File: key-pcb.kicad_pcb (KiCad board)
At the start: 2 copper layers, 3.6 x 3.3 mm, 24 parts, among them J1 row left, J10 DIN bottom, J11 DOUT bottom, J12 VDD bottom, J13 VSS left, J14 DOUT left, J15 DIN left, J16 VDD left, J17 VDD right, J18 DOUT right, J19 DIN right, J2 row right, J20 VSS right, J3 col top, J4 col bottom, J5 VDD top, J6 DIN top, J7 DOUT top, J8 VSS top, J9 VSS bottom

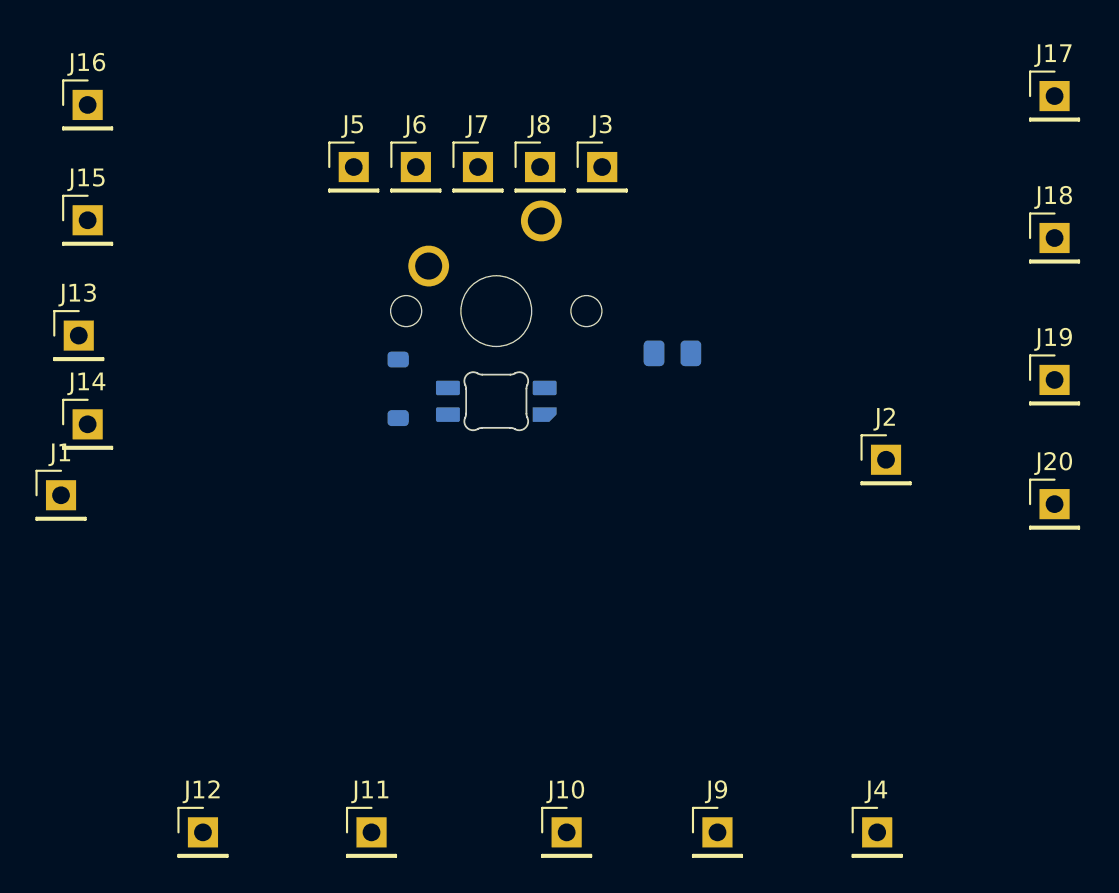
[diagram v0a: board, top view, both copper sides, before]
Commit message: Routed, but DRC violation
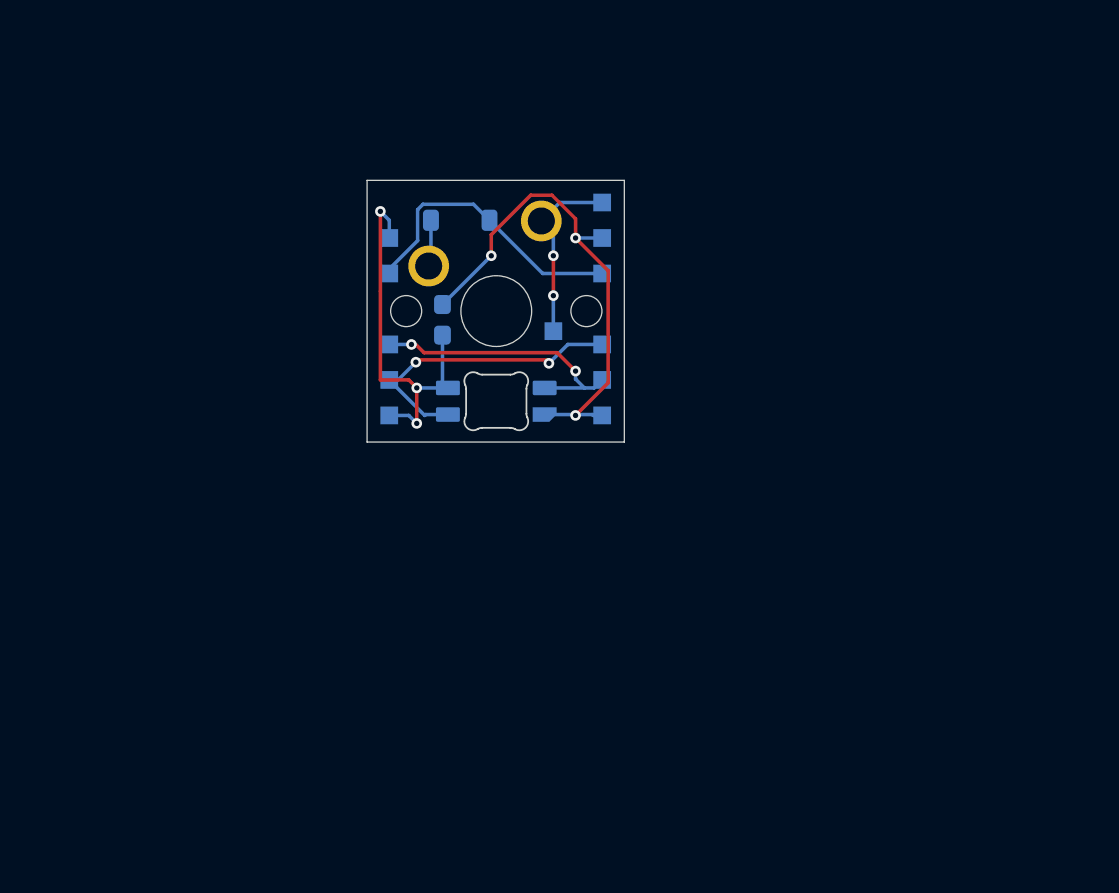
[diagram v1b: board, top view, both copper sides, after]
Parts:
- removed J10: DIN bottom, Connector_PinHeader_2.54mm:PinHeader_1x01_P2.54mm_Vertical
- removed J11: DOUT bottom, Connector_PinHeader_2.54mm:PinHeader_1x01_P2.54mm_Vertical
- removed J13: VSS left, Connector_PinHeader_2.54mm:PinHeader_1x01_P2.54mm_Vertical
- removed J16: VDD left, Connector_PinHeader_2.54mm:PinHeader_1x01_P2.54mm_Vertical
- removed J17: VDD right, Connector_PinHeader_2.54mm:PinHeader_1x01_P2.54mm_Vertical
- removed J20: VSS right, Connector_PinHeader_2.54mm:PinHeader_1x01_P2.54mm_Vertical
- removed J6: DIN top, Connector_PinHeader_2.54mm:PinHeader_1x01_P2.54mm_Vertical
- removed J7: DOUT top, Connector_PinHeader_2.54mm:PinHeader_1x01_P2.54mm_Vertical
- C1: footprint Capacitor_SMD:C_0805_2012Metric_Pad1.18x1.45mm_HandSolder -> Capacitor_SMD:C_0603_1608Metric_Pad1.08x0.95mm_HandSolder
- J1, J12, J14, J15, J18, J19, J2, J3, J4, J5, J8, J9: footprint Connector_PinHeader_2.54mm:PinHeader_1x01_P2.54mm_Vertical -> TestPoint:TestPoint_Pad_1.0x1.0mm; moved to B.Cu
- moved J4 33.6 mm to (141.2, 97.8), turned to 180 degrees
- moved J18 26.2 mm to (144.0, 98.5), turned to 180 degrees
- moved J12 25.7 mm to (132.0, 102.5), turned to 180 degrees
- moved J19 25.5 mm to (144.0, 100.5), turned to 180 degrees
- moved J9 24.4 mm to (144.0, 102.5), turned to 180 degrees
- moved J1 22.3 mm to (132.0, 94.5), turned to 180 degrees
- moved J2 19.1 mm to (144.0, 94.5), turned to 180 degrees
- moved J15 18.4 mm to (132.0, 98.5), turned to 180 degrees
- moved J14 17.2 mm to (132.0, 100.5), turned to 180 degrees
- moved C1 13.1 mm to (135.0, 97.1), turned to -90 degrees
- moved D1 10.1 mm to (136.0, 91.5), turned to 180 degrees
- moved J8 5.32 mm to (144.0, 92.5), turned to 180 degrees
- moved J5 4.47 mm to (132.0, 92.5), turned to 180 degrees
- moved J3 2.00 mm to (144.0, 90.5), turned to 180 degrees
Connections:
- net GND renamed VSS
- net Net-(D1-K) renamed /row
- net Net-(J10-Pin_1) renamed /DIN
- net Net-(J11-Pin_1) renamed /DOUT
- net Net-(J12-Pin_1) renamed VDD
- net Net-(J3-Pin_1) renamed /col
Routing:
- net VSS: track 0.00 -> 29.3 mm, vias 0 -> 3
- net VDD: track 0.00 -> 22.2 mm, vias 0 -> 3
- net /DOUT: track 0.00 -> 17.3 mm, vias 0 -> 2
- net /row: track 0.00 -> 16.4 mm
- net /DIN: track 0.00 -> 15.5 mm, vias 0 -> 2
- net /col: track 0.00 -> 10.3 mm, vias 0 -> 2
- net Net-(D1-A): track 0.00 -> 2.63 mm
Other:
- board size 3.6 x 3.3 mm -> 14.5 x 14.8 mm

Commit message: Passing all DRC
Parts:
- renumbered J5 to +, J12 to +, J8 to -, J9 to -, D1 to D, J19 to IN, J15 to IN, LED1 to LED, J18 to OUT, J14 to OUT, J4 to c, J3 to c, C1 to cap, J1 to r, J2 to r
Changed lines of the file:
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@@
 		(descr "Add-on for regular MX-footprints with 6028 reverse mount LED")
 		(tags "cherry MX 6028 rearmount rear mount led rgb backlight")
-		(property "Reference" "LED1"
-			(at 0.5 -2.6 0)
-			(layer "B.SilkS")
-			(effects
-				(font
-					(size 1 1)
-					(thickness 0.15)
+		(property "Reference" "LED"
+			(at 0.0325 2.2 0)
+			(layer "B.SilkS")
+			(effects
+				(font
+					(size 0.8 0.8)
+					(thickness 0.125)
 				)
 				(justify mirror)
@@
 		(descr "SMD rectangular pad as test Point, square 1.0mm side length")
 		(tags "test point SMD pad rectangle square")
-		(property "Reference" "J19"
-			(at 0 1.448 0)
-			(layer "B.SilkS")
-			(effects
-				(font
-					(size 1 1)
-					(thickness 0.15)
+		(property "Reference" "IN"
+			(at 1.5 0 0)
+			(layer "B.SilkS")
+			(effects
+				(font
+					(size 0.8 0.8)
+					(thickness 0.125)
+					(bold yes)
 				)
 				(justify mirror)
@@
 		(descr "SMD rectangular pad as test Point, square 1.0mm side length")
 		(tags "test point SMD pad rectangle square")
-		(property "Reference" "J18"
-			(at 0 1.448 0)
-			(layer "B.SilkS")
-			(effects
-				(font
-					(size 1 1)
-					(thickness 0.15)
+		(property "Reference" "OUT"
+			(at 2 -0.75 0)
+			(layer "B.SilkS")
+			(effects
+				(font
+					(size 0.8 0.8)
+					(thickness 0.125)
+					(bold yes)
 				)
 				(justify mirror)
@@
 		(descr "Capacitor SMD 0603 (1608 Metric), square (rectangular) end terminal, IPC-7351 nominal with elongated pad for handsoldering. (Body size source: IPC-SM-782 page 76, https://www.pcb-3d.com/wordpress/wp-content/uploads/ipc-sm-782a_amendment_1_and_2.pdf), generated with kicad-footprint-generator")
 		(tags "capacitor handsolder")
-		(property "Reference" "C1"
-			(at 0 1.43 90)
-			(layer "B.SilkS")
-			(effects
-				(font
-					(size 1 1)
-					(thickness 0.15)
+		(property "Reference" "cap"
+			(at -2.6125 -0.75 90)
+			(layer "B.SilkS")
+			(effects
+				(font
+					(size 0.8 0.8)
+					(thickness 0.125)
+					(bold yes)
 				)
 				(justify mirror)
@@
 		(descr "SMD rectangular pad as test Point, square 1.0mm side length")
 		(tags "test point SMD pad rectangle square")
-		(property "Reference" "J8"
-			(at 0 1.448 0)
-			(layer "B.SilkS")
-			(effects
-				(font
-					(size 1 1)
-					(thickness 0.15)
+		(property "Reference" "-"
+			(at 1.5 0 0)
+			(layer "B.SilkS")
+			(effects
+				(font
+					(size 0.8 0.8)
+					(thickness 0.125)
 				)
 				(justify mirror)
@@
 		(descr "SMD rectangular pad as test Point, square 1.0mm side length")
 		(tags "test point SMD pad rectangle square")
-		(property "Reference" "J1"
-			(at 0 1.448 0)
-			(layer "B.SilkS")
-			(effects
-				(font
-					(size 1 1)
-					(thickness 0.15)
+		(property "Reference" "r"
+			(at -1 -0.539554 0)
+			(layer "B.SilkS")
+			(effects
+				(font
+					(size 0.8 0.8)
+					(thickness 0.125)
+					(bold yes)
 				)
 				(justify mirror)
@@
 		(descr "SMD rectangular pad as test Point, square 1.0mm side length")
 		(tags "test point SMD pad rectangle square")
-		(property "Reference" "J5"
-			(at 0 1.448 0)
-			(layer "B.SilkS")
-			(effects
-				(font
-					(size 1 1)
-					(thickness 0.15)
+		(property "Reference" "+"
+			(at -1.25 0 0)
+			(layer "B.SilkS")
+			(effects
+				(font
+					(size 0.8 0.8)
+					(thickness 0.125)
+					(bold yes)
 				)
 				(justify mirror)
@@
 		(descr "SMD rectangular pad as test Point, square 1.0mm side length")
 		(tags "test point SMD pad rectangle square")
-		(property "Reference" "J9"
-			(at 0 1.448 0)
-			(layer "B.SilkS")
-			(effects
-				(font
-					(size 1 1)
-					(thickness 0.15)
+		(property "Reference" "-"
+			(at 1.75 0 0)
+			(layer "B.SilkS")
+			(effects
+				(font
+					(size 0.8 0.8)
+					(thickness 0.125)
+					(bold yes)
 				)
 				(justify mirror)
@@
 		(descr "SMD rectangular pad as test Point, square 1.0mm side length")
 		(tags "test point SMD pad rectangle square")
-		(property "Reference" "J4"
+		(property "Reference" "c"
 			(at 0 1.448 0)
 			(layer "B.SilkS")
 			(effects
 				(font
-					(size 1 1)
-					(thickness 0.15)
+					(size 0.8 0.8)
+					(thickness 0.125)
+					(bold yes)
 				)
 				(justify mirror)
@@
 		(descr "SMD rectangular pad as test Point, square 1.0mm side length")
 		(tags "test point SMD pad rectangle square")
-		(property "Reference" "J12"
-			(at 0 1.448 0)
-			(layer "B.SilkS")
-			(effects
-				(font
-					(size 1 1)
-					(thickness 0.15)
+		(property "Reference" "+"
+			(at -1.5 0.5 0)
+			(layer "B.SilkS")
+			(effects
+				(font
+					(size 0.8 0.8)
+					(thickness 0.125)
+					(bold yes)
 				)
 				(justify mirror)
@@
 		(descr "SMD rectangular pad as test Point, square 1.0mm side length")
 		(tags "test point SMD pad rectangle square")
-		(property "Reference" "J15"
-			(at 0 1.448 0)
-			(layer "B.SilkS")
-			(effects
-				(font
-					(size 1 1)
-					(thickness 0.15)
+		(property "Reference" "IN"
+			(at -1.75 0.5 0)
+			(layer "B.SilkS")
+			(effects
+				(font
+					(size 0.8 0.8)
+					(thickness 0.125)
+					(bold yes)
 				)
 				(justify mirror)
@@
 		(descr "SMD rectangular pad as test Point, square 1.0mm side length")
 		(tags "test point SMD pad rectangle square")
-		(property "Reference" "J2"
-			(at 0 1.448 0)
-			(layer "B.SilkS")
-			(effects
-				(font
-					(size 1 1)
-					(thickness 0.15)
+		(property "Reference" "r"
+			(at 1.5 0 0)
+			(layer "B.SilkS")
+			(effects
+				(font
+					(size 0.8 0.8)
+					(thickness 0.125)
+					(bold yes)
 				)
 				(justify mirror)
@@
 		(descr "SMD rectangular pad as test Point, square 1.0mm side length")
 		(tags "test point SMD pad rectangle square")
-		(property "Reference" "J14"
-			(at 0 1.448 0)
-			(layer "B.SilkS")
-			(effects
-				(font
-					(size 1 1)
-					(thickness 0.15)
+		(property "Reference" "OUT"
+			(at -2 0.5 0)
+			(layer "B.SilkS")
+			(effects
+				(font
+					(size 0.8 0.8)
+					(thickness 0.125)
+					(bold yes)
 				)
 				(justify mirror)
@@
 		(descr "SMD rectangular pad as test Point, square 1.0mm side length")
 		(tags "test point SMD pad rectangle square")
-		(property "Reference" "J3"
-			(at 0 1.448 0)
-			(layer "B.SilkS")
-			(effects
-				(font
-					(size 1 1)
-					(thickness 0.15)
+		(property "Reference" "c"
+			(at 1.25 0 0)
+			(layer "B.SilkS")
+			(effects
+				(font
+					(size 0.8 0.8)
+					(thickness 0.125)
 				)
 				(justify mirror)
@@
 		(descr "SOD-123")
 		(tags "SOD-123")
-		(property "Reference" "D1"
-			(at 0 2 0)
-			(layer "B.SilkS")
-			(effects
-				(font
-					(size 1 1)
-					(thickness 0.15)
-				)
-				(justify mirror)
+		(property "Reference" "D"
+			(at 0 0 0)
+			(layer "B.SilkS")
+			(effects
+				(font
+					(size 0.8 0.8)
+					(thickness 0.125)
+					(bold yes)
+				)
+				(justify mirror)

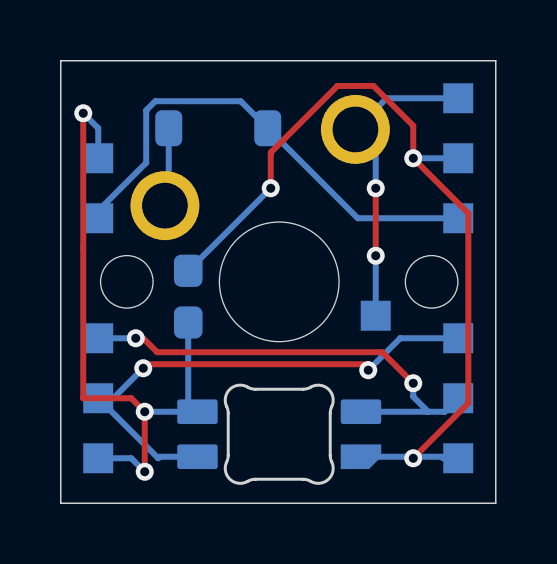
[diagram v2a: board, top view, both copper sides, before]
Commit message: Smaller board
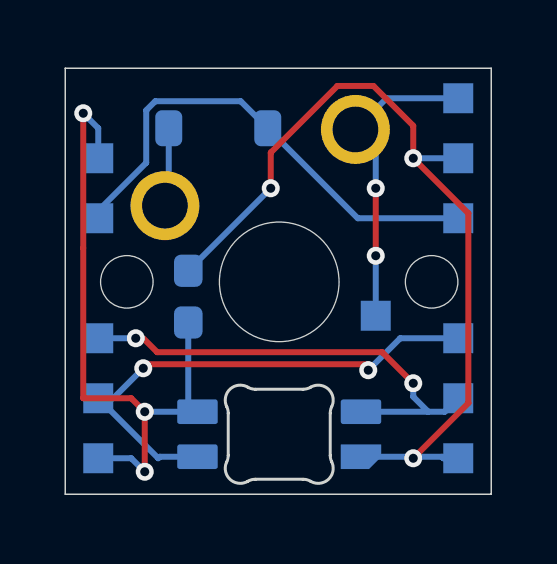
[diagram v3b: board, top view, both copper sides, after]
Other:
- board size 14.5 x 14.8 mm -> 14.2 x 14.2 mm
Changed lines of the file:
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@@
 	)
 	(gr_line
-		(start 130.75 89.25)
-		(end 145.25 89.25)
+		(start 130.9 89.5)
+		(end 145.1 89.5)
 		(stroke
 			(width 0.05)
@@
 	)
 	(gr_line
-		(start 145.25 104)
-		(end 130.75 104)
+		(start 145.1 103.699999)
+		(end 130.9 103.699999)
 		(stroke
 			(width 0.05)
@@
 	)
 	(gr_line
-		(start 145.25 89.25)
-		(end 145.25 104)
+		(start 145.1 89.5)
+		(end 145.1 103.699999)
 		(stroke
 			(width 0.05)
@@
 	)
 	(gr_line
-		(start 130.75 104)
-		(end 130.75 89.25)
+		(start 130.9 103.7)
+		(end 130.9 89.5)
 		(stroke
 			(width 0.05)

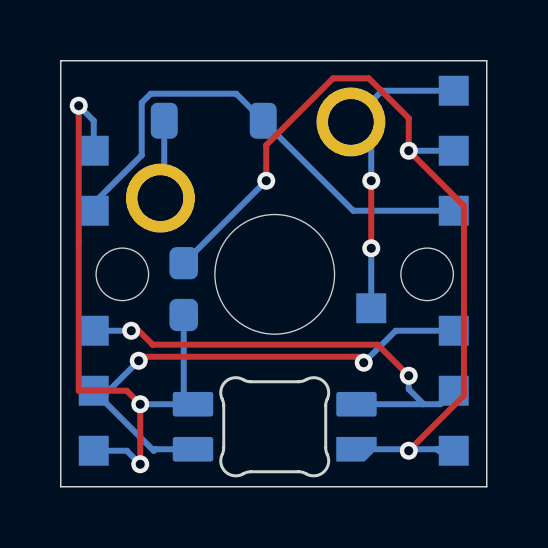
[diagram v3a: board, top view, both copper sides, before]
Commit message: Ground fill
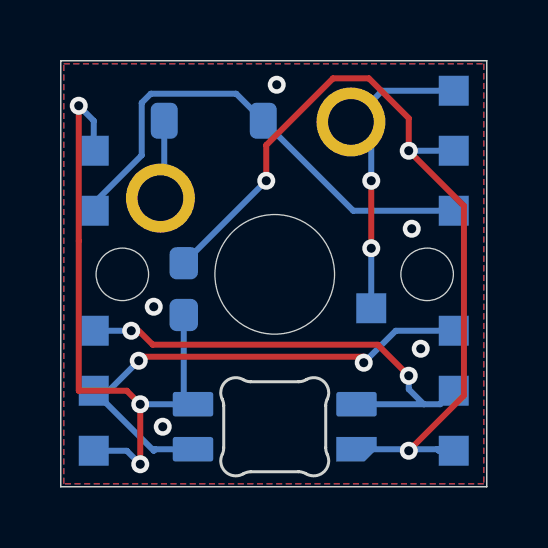
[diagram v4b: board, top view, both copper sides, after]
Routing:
- net VSS: vias 3 -> 8
- added copper zone on B.Cu, net VSS
- added copper zone on F.Cu, net VSS
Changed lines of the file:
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@@
+	)
+	(via
+		(at 142.9 99.1)
+		(size 0.6)
+		(drill 0.3)
+		(layers "F.Cu" "B.Cu")
+		(free yes)
+		(net 6)
 	)
 	(via
@@
 		(drill 0.3)
 		(layers "F.Cu" "B.Cu")
+		(net 6)
+	)
+	(via
+		(at 134.3 101.7)
+		(size 0.6)
+		(drill 0.3)
+		(layers "F.Cu" "B.Cu")
+		(free yes)
+		(net 6)
+	)
+	(via
+		(at 142.6 95.1)
+		(size 0.6)
+		(drill 0.3)
+		(layers "F.Cu" "B.Cu")
+		(free yes)
+		(net 6)
+	)
+	(via
+		(at 138.1 90.3)
+		(size 0.6)
+		(drill 0.3)
+		(layers "F.Cu" "B.Cu")
+		(free yes)
+		(net 6)
+	)
+	(via
+		(at 134 97.7)
+		(size 0.6)
+		(drill 0.3)
+		(layers "F.Cu" "B.Cu")
+		(free yes)
 		(net 6)
 	)
@@
 		(net 7)
 	)
+	(zone
+		(net 6)
+		(net_name "VSS")
+		(layer "F.Cu")
+		(hatch edge 0.5)
+		(connect_pads
+			(clearance 0.25)
+		)
+		(min_thickness 0.125)
+		(filled_areas_thickness no)
+		(fill yes
+			(thermal_gap 0.5)
+			(thermal_bridge_width 0.5)
+		)
+		(polygon
+			(pts
+				(xy 131 89.6) (xy 145 89.6) (xy 145 103.6) (xy 131 103.6)
+			)
+		)
+	)
+	(zone
+		(net 6)
+		(net_name "VSS")
+		(layer "B.Cu")
+		(hatch edge 0.5)
+		(priority 1)
+		(connect_pads
+			(clearance 0.25)
+		)
+		(min_thickness 0.125)
+		(filled_areas_thickness no)
+		(fill yes
+			(thermal_gap 0.5)
+			(thermal_bridge_width 0.5)
+		)
+		(polygon
+			(pts
+				(xy 131 89.6) (xy 145 89.6) (xy 145 103.6) (xy 131 103.6)
+			)
+		)
+	)
 	(embedded_fonts no)
